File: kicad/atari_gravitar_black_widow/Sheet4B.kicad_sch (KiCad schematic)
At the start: 45 parts

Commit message: PLACED C1-C15
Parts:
- C9: footprint (none) -> Star_Wars_Vector_PCB:GenericComp
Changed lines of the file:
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@@
       (effects (font (size 1.27 1.27)) (justify left))
     )
-    (property "Footprint" "" (id 2) (at 471.805 134.9248 0)
+    (property "Footprint" "Star_Wars_Vector_PCB:GenericComp" (id 2) (at 471.805 134.9248 0)
       (effects (font (size 1.27 1.27)) hide)
     )

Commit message: C16-30
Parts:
- C16: footprint (none) -> Star_Wars_Vector_PCB:LargeCap
- C17, C36, C38: footprint (none) -> Star_Wars_Vector_PCB:CapElec2
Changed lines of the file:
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@@
       (effects (font (size 1.27 1.27)) (justify left))
     )
-    (property "Footprint" "" (id 2) (at 451.8152 93.98 0)
+    (property "Footprint" "Star_Wars_Vector_PCB:CapElec2" (id 2) (at 451.8152 93.98 0)
       (effects (font (size 1.27 1.27)) hide)
     )
@@
       (effects (font (size 1.27 1.27)) (justify left))
     )
-    (property "Footprint" "" (id 2) (at 414.655 98.7298 0)
+    (property "Footprint" "Star_Wars_Vector_PCB:CapElec2" (id 2) (at 414.655 98.7298 0)
       (effects (font (size 1.27 1.27)) hide)
     )
@@
       (effects (font (size 1.27 1.27)) (justify left))
     )
-    (property "Footprint" "" (id 2) (at 439.7502 93.98 0)
+    (property "Footprint" "Star_Wars_Vector_PCB:LargeCap" (id 2) (at 439.7502 93.98 0)
       (effects (font (size 1.27 1.27)) hide)
     )
@@
       (effects (font (size 1.27 1.27)) (justify left))
     )
-    (property "Footprint" "" (id 2) (at 388.9502 90.805 0)
-      (effects (font (size 1.27 1.27)) hide)
-    )
+    (property "Footprint" "Star_Wars_Vector_PCB:CapElec2" (id 2) (at 388.9502 90.805 0)
+      (effects (font (size 1.27 1.27)) hide)
+    )

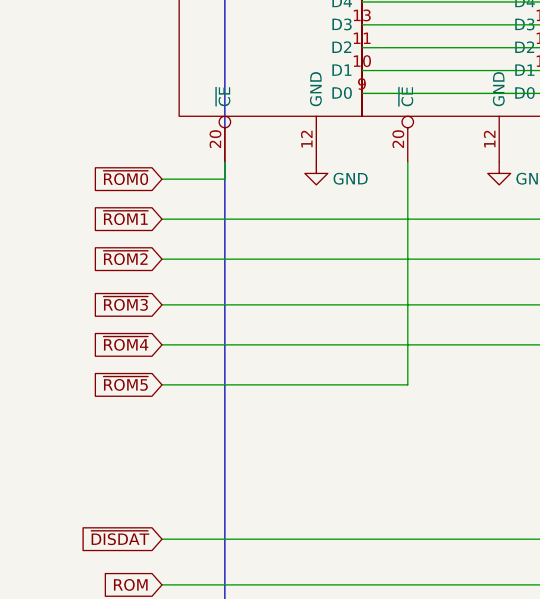
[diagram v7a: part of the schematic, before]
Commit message: Row one solder / ROM fix
ROM enables were shifted on schematic
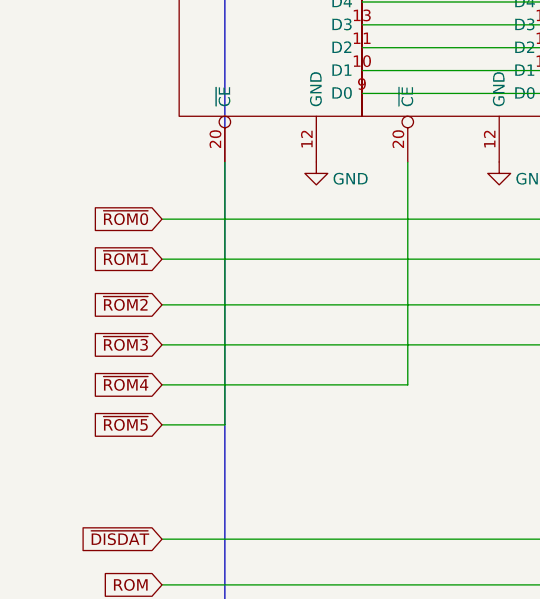
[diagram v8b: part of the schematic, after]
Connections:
- net ~{ROM0}: now also D_1.20 (~{CE}); no longer M_1.20 (~{CE})
- net ~{ROM1}: now also E/F_1.20 (~{CE}); no longer D_1.20 (~{CE})
- net ~{ROM2}: now also H_1.20 (~{CE}); no longer E/F_1.20 (~{CE})
- net ~{ROM3}: now also J_1.20 (~{CE}); no longer H_1.20 (~{CE})
- net ~{ROM4}: now also K/L_1.20 (~{CE}); no longer J_1.20 (~{CE})
- net ~{ROM5}: now also M_1.20 (~{CE}); no longer K/L_1.20 (~{CE})
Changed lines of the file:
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@@
     (stroke (width 0) (type default) (color 0 0 0 0))
   )
-  (wire (pts (xy 58.42 145.415) (xy 65.405 145.415))
+  (wire (pts (xy 58.42 172.72) (xy 65.405 172.72))
     (stroke (width 0) (type default) (color 0 0 0 0))
   )
@@
     (stroke (width 0) (type default) (color 0 0 0 0))
   )
-  (wire (pts (xy 65.405 143.51) (xy 65.405 145.415))
+  (wire (pts (xy 65.405 143.51) (xy 65.405 172.72))
     (stroke (width 0) (type default) (color 0 0 0 0))
   )
@@
     )
   )
-  (global_label "~{ROM4}" (shape input) (at 58.42 163.83 180) (fields_autoplaced)
-    (effects (font (size 1.27 1.27)) (justify right))
-    (property "Intersheet References" "${INTERSHEET_REFS}" (id 0) (at 50.8344 163.9094 0)
+  (global_label "~{ROM4}" (shape input) (at 58.42 168.275 180) (fields_autoplaced)
+    (effects (font (size 1.27 1.27)) (justify right))
+    (property "Intersheet References" "${INTERSHEET_REFS}" (id 0) (at 50.8344 168.3544 0)
       (effects (font (size 1.27 1.27)) (justify right) hide)
     )
@@
     )
   )
-  (global_label "~{ROM1}" (shape input) (at 58.42 149.86 180) (fields_autoplaced)
-    (effects (font (size 1.27 1.27)) (justify right))
-    (property "Intersheet References" "${INTERSHEET_REFS}" (id 0) (at 50.8344 149.9394 0)
+  (global_label "~{ROM1}" (shape input) (at 58.42 154.305 180) (fields_autoplaced)
+    (effects (font (size 1.27 1.27)) (justify right))
+    (property "Intersheet References" "${INTERSHEET_REFS}" (id 0) (at 50.8344 154.3844 0)
       (effects (font (size 1.27 1.27)) (justify right) hide)
     )
@@
     )
   )
-  (global_label "~{ROM5}" (shape input) (at 58.42 168.275 180) (fields_autoplaced)
-    (effects (font (size 1.27 1.27)) (justify right))
-    (property "Intersheet References" "${INTERSHEET_REFS}" (id 0) (at 50.8344 168.3544 0)
+  (global_label "~{ROM5}" (shape input) (at 58.42 172.72 180) (fields_autoplaced)
+    (effects (font (size 1.27 1.27)) (justify right))
+    (property "Intersheet References" "${INTERSHEET_REFS}" (id 0) (at 50.8344 172.7994 0)
       (effects (font (size 1.27 1.27)) (justify right) hide)
     )
@@
     )
   )
-  (global_label "~{ROM3}" (shape input) (at 58.42 159.385 180) (fields_autoplaced)
+  (global_label "~{ROM3}" (shape input) (at 58.42 163.83 180) (fields_autoplaced)
+    (effects (font (size 1.27 1.27)) (justify right))
+    (property "Intersheet References" "${INTERSHEET_REFS}" (id 0) (at 50.8344 163.9094 0)
+      (effects (font (size 1.27 1.27)) (justify right) hide)
+    )
+  )
+  (global_label "12KHZ" (shape input) (at 347.345 90.17 180) (fields_autoplaced)
+    (effects (font (size 1.27 1.27)) (justify right))
+    (property "Intersheet References" "${INTERSHEET_REFS}" (id 0) (at 338.7918 90.0906 0)
+      (effects (font (size 1.27 1.27)) (justify right) hide)
+    )
+  )
+  (global_label "DB3" (shape input) (at 546.735 198.12 0) (fields_autoplaced)
+    (effects (font (size 1.27 1.27)) (justify left))
+    (property "Intersheet References" "${INTERSHEET_REFS}" (id 0) (at 552.8087 198.0406 0)
+      (effects (font (size 1.27 1.27)) (justify left) hide)
+    )
+  )
+  (global_label "AB1" (shape input) (at 50.8 111.76 180) (fields_autoplaced)
+    (effects (font (size 1.27 1.27)) (justify right))
+    (property "Intersheet References" "${INTERSHEET_REFS}" (id 0) (at 44.9077 111.6806 0)
+      (effects (font (size 1.27 1.27)) (justify right) hide)
+    )
+  )
+  (global_label "DB4" (shape input) (at 234.95 299.72 0) (fields_autoplaced)
+    (effects (font (size 1.27 1.27)) (justify left))
+    (property "Intersheet References" "${INTERSHEET_REFS}" (id 0) (at 241.0237 299.6406 0)
+      (effects (font (size 1.27 1.27)) (justify left) hide)
+    )
+  )
+  (global_label "AB11" (shape input) (at 50.8 86.36 180) (fields_autoplaced)
+    (effects (font (size 1.27 1.27)) (justify right))
+    (property "Intersheet References" "${INTERSHEET_REFS}" (id 0) (at 43.6982 86.2806 0)
+      (effects (font (size 1.27 1.27)) (justify right) hide)
+    )
+  )
+  (global_label "AB1" (shape input) (at 347.345 161.29 180) (fields_autoplaced)
+    (effects (font (size 1.27 1.27)) (justify right))
+    (property "Intersheet References" "${INTERSHEET_REFS}" (id 0) (at 341.4527 161.2106 0)
+      (effects (font (size 1.27 1.27)) (justify right) hide)
+    )
+  )
+  (global_label "~{EAROMWR}" (shape input) (at 346.075 287.02 180) (fields_autoplaced)
+    (effects (font (size 1.27 1.27)) (justify right))
+    (property "Intersheet References" "${INTERSHEET_REFS}" (id 0) (at 334.7398 286.9406 0)
+      (effects (font (size 1.27 1.27)) (justify right) hide)
+    )
+  )
+  (global_label "DB2" (shape input) (at 546.735 200.66 0) (fields_autoplaced)
+    (effects (font (size 1.27 1.27)) (justify left))
+    (property "Intersheet References" "${INTERSHEET_REFS}" (id 0) (at 552.8087 200.5806 0)
+      (effects (font (size 1.27 1.27)) (justify left) hide)
+    )
+  )
+  (global_label "DB5" (shape input) (at 234.95 297.18 0) (fields_autoplaced)
+    (effects (font (size 1.27 1.27)) (justify left))
+    (property "Intersheet References" "${INTERSHEET_REFS}" (id 0) (at 241.0237 297.1006 0)
+      (effects (font (size 1.27 1.27)) (justify left) hide)
+    )
+  )
+  (global_label "~{ROM2}" (shape input) (at 58.42 159.385 180) (fields_autoplaced)
     (effects (font (size 1.27 1.27)) (justify right))
     (property "Intersheet References" "${INTERSHEET_REFS}" (id 0) (at 50.8344 159.4644 0)
@@
     )
   )
-  (global_label "12KHZ" (shape input) (at 347.345 90.17 180) (fields_autoplaced)
-    (effects (font (size 1.27 1.27)) (justify right))
-    (property "Intersheet References" "${INTERSHEET_REFS}" (id 0) (at 338.7918 90.0906 0)
-      (effects (font (size 1.27 1.27)) (justify right) hide)
-    )
-  )
-  (global_label "DB3" (shape input) (at 546.735 198.12 0) (fields_autoplaced)
-    (effects (font (size 1.27 1.27)) (justify left))
-    (property "Intersheet References" "${INTERSHEET_REFS}" (id 0) (at 552.8087 198.0406 0)
-      (effects (font (size 1.27 1.27)) (justify left) hide)
-    )
-  )
-  (global_label "AB1" (shape input) (at 50.8 111.76 180) (fields_autoplaced)
-    (effects (font (size 1.27 1.27)) (justify right))
-    (property "Intersheet References" "${INTERSHEET_REFS}" (id 0) (at 44.9077 111.6806 0)
-      (effects (font (size 1.27 1.27)) (justify right) hide)
-    )
-  )
-  (global_label "DB4" (shape input) (at 234.95 299.72 0) (fields_autoplaced)
-    (effects (font (size 1.27 1.27)) (justify left))
-    (property "Intersheet References" "${INTERSHEET_REFS}" (id 0) (at 241.0237 299.6406 0)
-      (effects (font (size 1.27 1.27)) (justify left) hide)
-    )
-  )
-  (global_label "AB11" (shape input) (at 50.8 86.36 180) (fields_autoplaced)
-    (effects (font (size 1.27 1.27)) (justify right))
-    (property "Intersheet References" "${INTERSHEET_REFS}" (id 0) (at 43.6982 86.2806 0)
-      (effects (font (size 1.27 1.27)) (justify right) hide)
-    )
-  )
-  (global_label "AB1" (shape input) (at 347.345 161.29 180) (fields_autoplaced)
-    (effects (font (size 1.27 1.27)) (justify right))
-    (property "Intersheet References" "${INTERSHEET_REFS}" (id 0) (at 341.4527 161.2106 0)
-      (effects (font (size 1.27 1.27)) (justify right) hide)
-    )
-  )
-  (global_label "~{EAROMWR}" (shape input) (at 346.075 287.02 180) (fields_autoplaced)
-    (effects (font (size 1.27 1.27)) (justify right))
-    (property "Intersheet References" "${INTERSHEET_REFS}" (id 0) (at 334.7398 286.9406 0)
-      (effects (font (size 1.27 1.27)) (justify right) hide)
-    )
-  )
-  (global_label "DB2" (shape input) (at 546.735 200.66 0) (fields_autoplaced)
-    (effects (font (size 1.27 1.27)) (justify left))
-    (property "Intersheet References" "${INTERSHEET_REFS}" (id 0) (at 552.8087 200.5806 0)
-      (effects (font (size 1.27 1.27)) (justify left) hide)
-    )
-  )
-  (global_label "DB5" (shape input) (at 234.95 297.18 0) (fields_autoplaced)
-    (effects (font (size 1.27 1.27)) (justify left))
-    (property "Intersheet References" "${INTERSHEET_REFS}" (id 0) (at 241.0237 297.1006 0)
-      (effects (font (size 1.27 1.27)) (justify left) hide)
-    )
-  )
-  (global_label "~{ROM2}" (shape input) (at 58.42 154.305 180) (fields_autoplaced)
-    (effects (font (size 1.27 1.27)) (justify right))
-    (property "Intersheet References" "${INTERSHEET_REFS}" (id 0) (at 50.8344 154.3844 0)
-      (effects (font (size 1.27 1.27)) (justify right) hide)
-    )
-  )
   (global_label "AB4" (shape input) (at 58.42 302.26 180) (fields_autoplaced)
     (effects (font (size 1.27 1.27)) (justify right))
@@
     )
   )
-  (global_label "~{ROM0}" (shape input) (at 58.42 145.415 180) (fields_autoplaced)
-    (effects (font (size 1.27 1.27)) (justify right))
-    (property "Intersheet References" "${INTERSHEET_REFS}" (id 0) (at 50.8344 145.4944 0)
-      (effects (font (size 1.27 1.27)) (justify right) hide)
-    )
+  (global_label "~{ROM0}" (shape input) (at 58.42 149.86 180) (fields_autoplaced)
+    (effects (font (size 1.27 1.27)) (justify right))
+    (property "Intersheet References" "${INTERSHEET_REFS}" (id 0) (at 50.8344 149.9394 0)
+      (effects (font (size 1.27 1.27)) (justify right) hide)
+    )
